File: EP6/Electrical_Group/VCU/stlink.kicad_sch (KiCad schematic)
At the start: 33 parts, among them J16 STDC14, J2 Conn_01x06, J24 USB_C_stm32, SW1 VBUS, SW2 VBUS, U1 USB3300-EZK, U14 LM66100DCK, U15 USBLC6-2SC6, Y3 X322524MSB4SI

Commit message: add silkscreen on VCU PCB
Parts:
- J16: footprint Connector_PinHeader_1.27mm:PinHeader_2x07_P1.27mm_Vertical -> nturt_kicad_lib_EP6:box_header_14P_pitch127
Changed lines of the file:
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@@
 			)
 		)
-		(property "Footprint" "Connector_PinHeader_1.27mm:PinHeader_2x07_P1.27mm_Vertical"
+		(property "Footprint" "nturt_kicad_lib_EP6:box_header_14P_pitch127"
 			(at 39.37 137.16 0)
 			(effects

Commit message: VCU snapshot
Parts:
- added R2: 100R, Resistor_SMD:R_0402_1005Metric, symbol Device:R_Small
- J2, SW2: now not fitted; now left out of the parts list
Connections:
- net 3V3_stlinkv3 is gone; now on net +3V3: J16.3 (Pin_3), SW2.1 (A)
- net GND: now also R2.1
- net at J16.11 (Pin_11): now also R2.2
- no-connect marks 13 -> 12
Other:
- note removed: "GNDDetect"
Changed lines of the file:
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@@
 	)
 	(junction
+		(at 26.67 132.08)
+		(diameter 0)
+		(color 0 0 0 0)
+	)
+	(junction
 		(at 64.77 50.8)
 		(diameter 0)
@@
 		(at 34.29 129.54)
 	)
-	(no_connect
-		(at 34.29 142.24)
-	)
 	(bus_entry
 		(at 194.31 126.746)
@@
 	(wire
 		(pts
+			(xy 21.59 142.24) (xy 34.29 142.24)
+		)
+		(stroke
+			(width 0)
+			(type default)
+		)
+	)
+	(wire
+		(pts
 			(xy 245.11 68.58) (xy 255.27 68.58)
 		)
@@
 	(wire
 		(pts
+			(xy 24.13 132.08) (xy 26.67 132.08)
+		)
+		(stroke
+			(width 0)
+			(type default)
+		)
+	)
+	(wire
+		(pts
 			(xy 242.57 27.94) (xy 255.27 27.94)
 		)
@@
 	(wire
 		(pts
+			(xy 15.24 142.24) (xy 16.51 142.24)
+		)
+		(stroke
+			(width 0)
+			(type default)
+		)
+	)
+	(wire
+		(pts
 			(xy 157.48 142.24) (xy 157.48 140.97)
 		)
@@
 		)
 	)
-	(text "GNDDetect"
-		(exclude_from_sim no)
-		(at 27.432 141.986 0)
-		(effects
-			(font
-				(size 1.27 1.27)
-			)
-		)
-	)
 	(text "NC"
 		(exclude_from_sim no)
@@
 		(at 53.34 118.11 180)
 		(unit 1)
-		(exclude_from_sim no)
-		(in_bom yes)
-		(on_board yes)
-		(dnp no)
+		(exclude_from_sim yes)
+		(in_bom no)
+		(on_board no)
+		(dnp yes)
 		(property "Reference" "SW2"
 			(at 53.34 110.49 0)
@@
 	(symbol
 		(lib_id "Device:R_Small")
+		(at 19.05 142.24 90)
+		(unit 1)
+		(exclude_from_sim no)
+		(in_bom yes)
+		(on_board yes)
+		(dnp no)
+		(fields_autoplaced yes)
+		(property "Reference" "R2"
+			(at 19.05 137.16 90)
+			(effects
+				(font
+					(size 1.27 1.27)
+				)
+			)
+		)
+		(property "Value" "100R"
+			(at 19.05 139.7 90)
+			(effects
+				(font
+					(size 1.27 1.27)
+				)
+			)
+		)
+		(property "Footprint" "Resistor_SMD:R_0402_1005Metric"
+			(at 19.05 142.24 0)
+			(effects
+				(font
+					(size 1.27 1.27)
+				)
+				(hide yes)
+			)
+		)
+		(property "Datasheet" "~"
+			(at 19.05 142.24 0)
+			(effects
+				(font
+					(size 1.27 1.27)
+				)
+				(hide yes)
+			)
+		)
+		(property "Description" "Resistor, small symbol"
+			(at 19.05 142.24 0)
+			(effects
+				(font
+					(size 1.27 1.27)
+				)
+				(hide yes)
+			)
+		)
+		(pin "2"
+		)
+		(pin "1"
+		)
+		(instances
+			(project ""
+				(path "/eb296f24-894e-4ea0-b0cd-3ba211155378/8cfc0c25-167d-4741-83fd-c9c2a0704b89"
+					(reference "R2")
+					(unit 1)
+				)
+			)
+		)
+	)
+	(symbol
+		(lib_id "Device:R_Small")
 		(at 257.81 25.4 90)
 		(unit 1)
@@
 	)
 	(symbol
+		(lib_id "power:GND")
+		(at 15.24 142.24 270)
+		(unit 1)
+		(exclude_from_sim no)
+		(in_bom yes)
+		(on_board yes)
+		(dnp no)
+		(fields_autoplaced yes)
+		(property "Reference" "#PWR042"
+			(at 8.89 142.24 0)
+			(effects
+				(font
+					(size 1.27 1.27)
+				)
+				(hide yes)
+			)
+		)
+		(property "Value" "GND"
+			(at 10.16 142.24 0)
+			(effects
+				(font
+					(size 1.27 1.27)
+				)
+				(hide yes)
+			)
+		)
+		(property "Footprint" ""
+			(at 15.24 142.24 0)
+			(effects
+				(font
+					(size 1.27 1.27)
+				)
+				(hide yes)
+			)
+		)
+		(property "Datasheet" ""
+			(at 15.24 142.24 0)
+			(effects
+				(font
+					(size 1.27 1.27)
+				)
+				(hide yes)
+			)
+		)
+		(property "Description" "Power symbol creates a global label with name \"GND\" , ground"
+			(at 15.24 142.24 0)
+			(effects
+				(font
+					(size 1.27 1.27)
+				)
+				(hide yes)
+			)
+		)
+		(pin "1"
+		)
+		(instances
+			(project "VCU"
+				(path "/eb296f24-894e-4ea0-b0cd-3ba211155378/8cfc0c25-167d-4741-83fd-c9c2a0704b89"
+					(reference "#PWR042")
+					(unit 1)
+				)
+			)
+		)
+	)
+	(symbol
 		(lib_id "Device:Crystal_GND24")
 		(at 102.87 107.95 0)
@@
 	)
 	(symbol
+		(lib_id "power:+3V3")
+		(at 24.13 132.08 90)
+		(unit 1)
+		(exclude_from_sim no)
+		(in_bom yes)
+		(on_board yes)
+		(dnp no)
+		(fields_autoplaced yes)
+		(property "Reference" "#PWR04"
+			(at 27.94 132.08 0)
+			(effects
+				(font
+					(size 1.27 1.27)
+				)
+				(hide yes)
+			)
+		)
+		(property "Value" "+3V3"
+			(at 20.32 132.0799 90)
+			(effects
+				(font
+					(size 1.27 1.27)
+				)
+				(justify left)
+			)
+		)
+		(property "Footprint" ""
+			(at 24.13 132.08 0)
+			(effects
+				(font
+					(size 1.27 1.27)
+				)
+				(hide yes)
+			)
+		)
+		(property "Datasheet" ""
+			(at 24.13 132.08 0)
+			(effects
+				(font
+					(size 1.27 1.27)
+				)
+				(hide yes)
+			)
+		)
+		(property "Description" "Power symbol creates a global label with name \"+3V3\""
+			(at 24.13 132.08 0)
+			(effects
+				(font
+					(size 1.27 1.27)
+				)
+				(hide yes)
+			)
+		)
+		(pin "1"
+		)
+		(instances
+			(project "VCU"
+				(path "/eb296f24-894e-4ea0-b0cd-3ba211155378/8cfc0c25-167d-4741-83fd-c9c2a0704b89"
+					(reference "#PWR04")
+					(unit 1)
+				)
+			)
+		)
+	)
+	(symbol
 		(lib_id "Power_Management:LM66100DCK")
 		(at 110.49 36.83 0)
@@
 		(at 38.1 102.87 180)
 		(unit 1)
-		(exclude_from_sim no)
-		(in_bom yes)
-		(on_board yes)
-		(dnp no)
+		(exclude_from_sim yes)
+		(in_bom no)
+		(on_board no)
+		(dnp yes)
 		(fields_autoplaced yes)
 		(property "Reference" "J2"

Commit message: VCU snapshot
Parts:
- R18, R52, R99: footprint Resistor_SMD:R_0603_1608Metric -> Resistor_SMD:R_0402_1005Metric
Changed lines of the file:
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@@
 			)
 		)
-		(property "Footprint" "Resistor_SMD:R_0603_1608Metric"
+		(property "Footprint" "Resistor_SMD:R_0402_1005Metric"
 			(at 259.08 111.252 90)
 			(effects
@@
 			)
 		)
-		(property "Footprint" "Resistor_SMD:R_0603_1608Metric"
+		(property "Footprint" "Resistor_SMD:R_0402_1005Metric"
 			(at 259.08 112.268 90)
 			(effects
@@
 			)
 		)
-		(property "Footprint" "Resistor_SMD:R_0603_1608Metric"
+		(property "Footprint" "Resistor_SMD:R_0402_1005Metric"
 			(at 125.222 137.16 90)
 			(effects

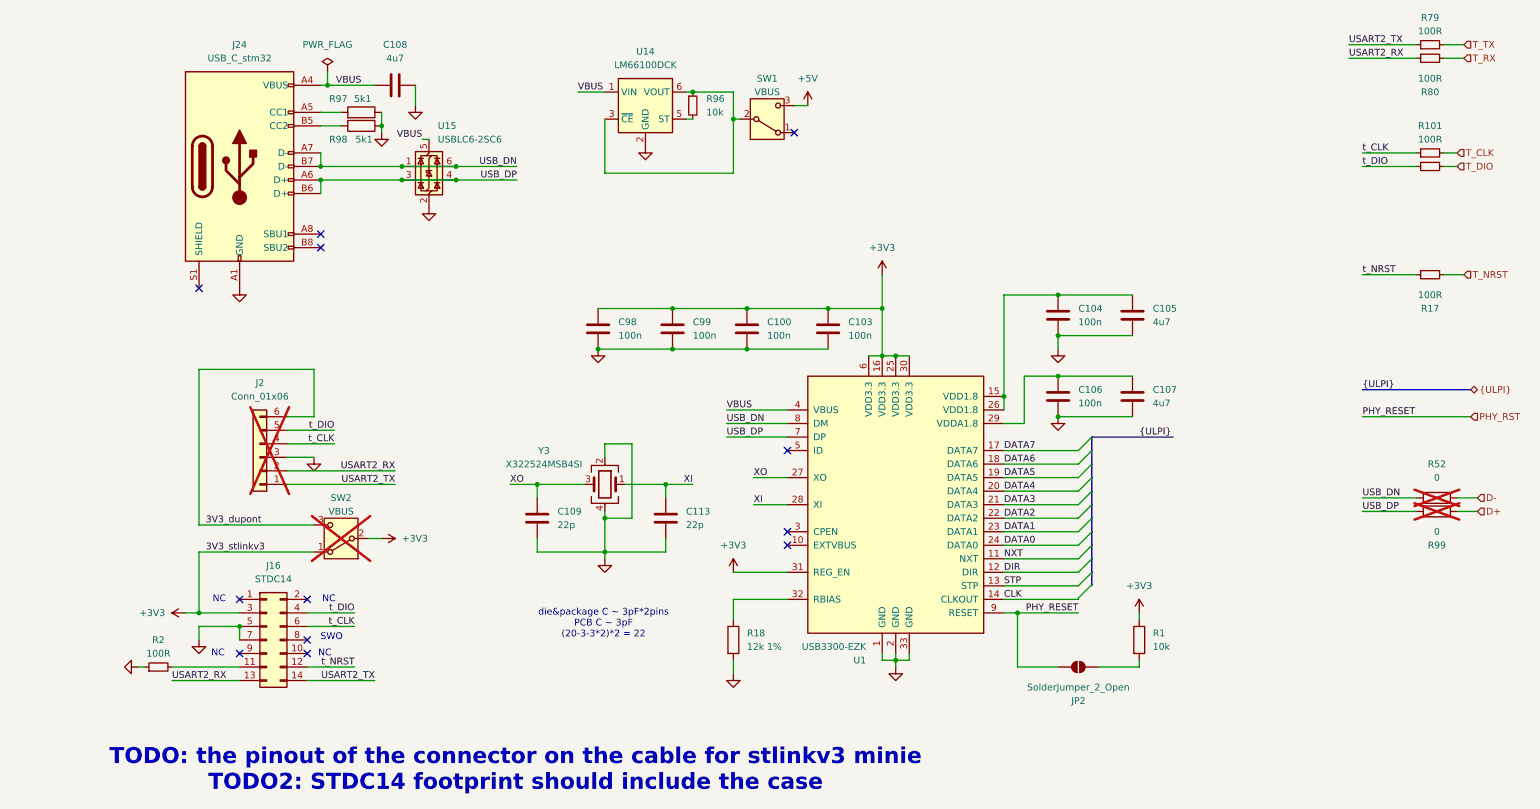
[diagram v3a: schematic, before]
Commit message: VCU initial layout
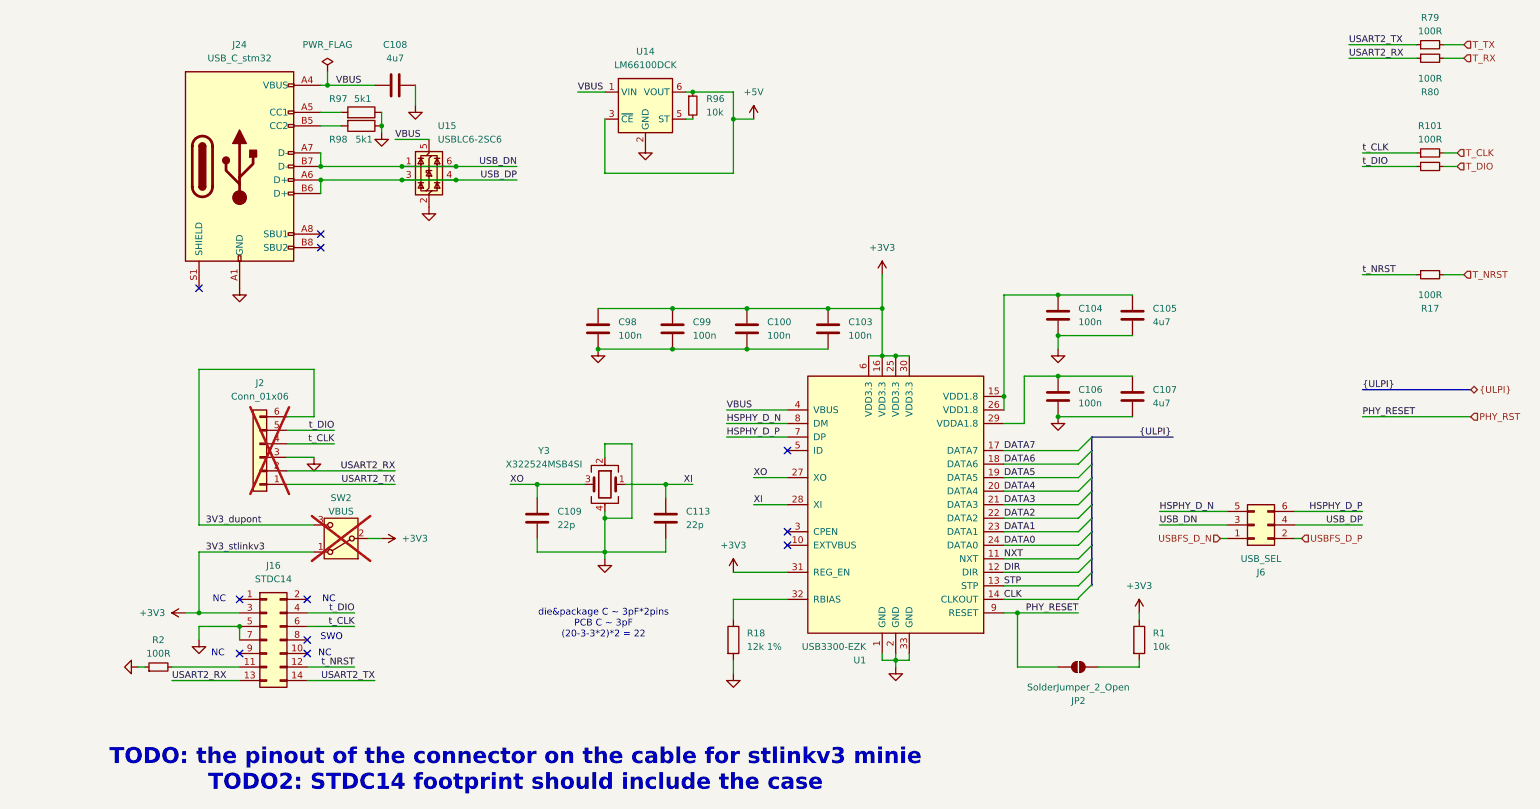
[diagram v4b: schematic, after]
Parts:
- removed R52, R99: 0, Resistor_SMD:R_0402_1005Metric, symbol Device:R
- removed SW1: VBUS, Connector_PinHeader_2.54mm:PinHeader_1x03_P2.54mm_Vertical, symbol Switch:SW_SPDT
- added J6: USB_SEL, Connector_PinHeader_2.54mm:PinHeader_2x03_P2.54mm_Vertical_SMD, symbol Connector_Generic:Conn_02x03_Odd_Even
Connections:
- net +5V: now also R96.1, U14.3 (~{CE}), U14.6 (VOUT)
- net USB_DN: now also J6.3 (Pin_3); no longer U1.8 (DM)
- net USB_DP: now also J6.4 (Pin_4); no longer U1.7 (DP)
- new net HSPHY_D_N: J6.5 (Pin_5), U1.8 (DM)
- new net HSPHY_D_P: J6.6 (Pin_6), U1.7 (DP)
- new net USBFS_D_N: J6.1 (Pin_1)
- new net USBFS_D_P: J6.2 (Pin_2)
- no-connect marks 12 -> 11

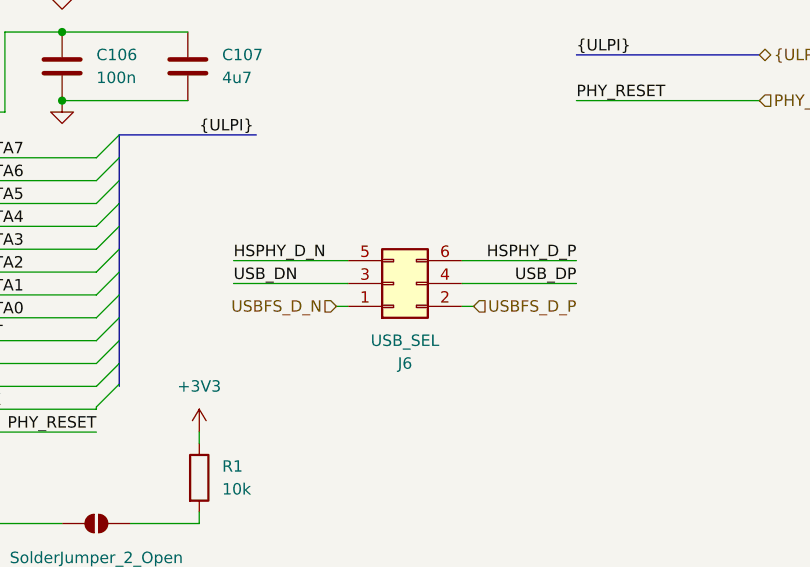
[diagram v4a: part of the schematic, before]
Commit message: VCU added silkscreen, added transfer vias, fixed ULP trace impedance
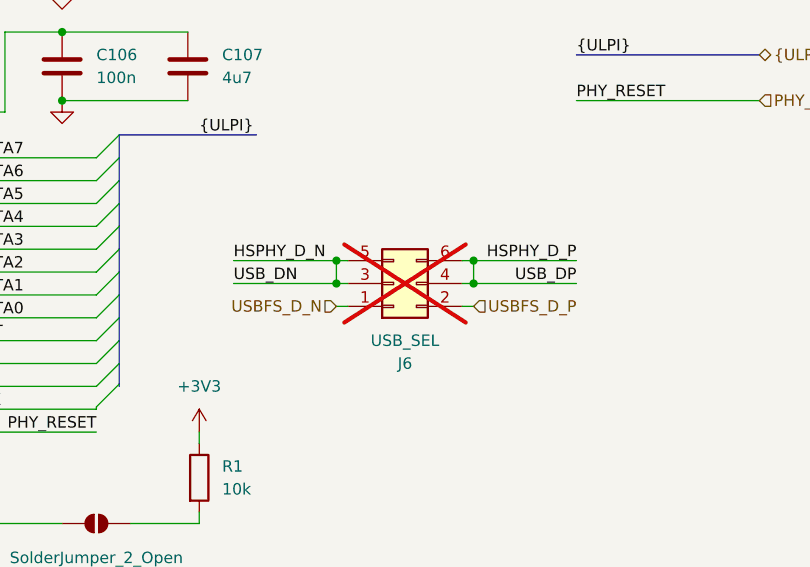
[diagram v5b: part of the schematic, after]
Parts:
- J6: now not fitted
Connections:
- net USB_DN is gone; now on net HSPHY_D_N: J24.A7 (D-), J24.B7 (D-), J6.3 (Pin_3), U15.1 (I/O1), U15.6 (I/O1)
- net USB_DP is gone; now on net HSPHY_D_P: J24.A6 (D+), J24.B6 (D+), J6.4 (Pin_4), U15.3 (I/O2), U15.4 (I/O2)
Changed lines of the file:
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@@
 	)
 	(junction
+		(at 233.68 115.57)
+		(diameter 0)
+		(color 0 0 0 0)
+	)
+	(junction
 		(at 49.53 50.8)
 		(diameter 0)
@@
 	)
 	(junction
+		(at 233.68 113.03)
+		(diameter 0)
+		(color 0 0 0 0)
+	)
+	(junction
 		(at 154.94 74.93)
 		(diameter 0)
@@
 	)
 	(junction
+		(at 218.44 113.03)
+		(diameter 0)
+		(color 0 0 0 0)
+	)
+	(junction
 		(at 115.57 82.55)
 		(diameter 0)
@@
 	)
 	(junction
+		(at 218.44 115.57)
+		(diameter 0)
+		(color 0 0 0 0)
+	)
+	(junction
 		(at 119.38 34.29)
 		(diameter 0)
@@
 	(wire
 		(pts
-			(xy 232.41 115.57) (xy 245.11 115.57)
+			(xy 232.41 115.57) (xy 233.68 115.57)
 		)
 		(stroke
@@
 	(wire
 		(pts
+			(xy 218.44 115.57) (xy 219.71 115.57)
+		)
+		(stroke
+			(width 0)
+			(type default)
+		)
+	)
+	(wire
+		(pts
 			(xy 64.77 50.8) (xy 74.93 50.8)
 		)
@@
 	(wire
 		(pts
+			(xy 218.44 113.03) (xy 219.71 113.03)
+		)
+		(stroke
+			(width 0)
+			(type default)
+		)
+	)
+	(wire
+		(pts
 			(xy 137.16 129.54) (xy 127 129.54)
 		)
@@
 	(wire
 		(pts
+			(xy 218.44 113.03) (xy 218.44 115.57)
+		)
+		(stroke
+			(width 0)
+			(type default)
+		)
+	)
+	(wire
+		(pts
 			(xy 130.81 111.76) (xy 137.16 111.76)
 		)
@@
 	(wire
 		(pts
+			(xy 233.68 115.57) (xy 245.11 115.57)
+		)
+		(stroke
+			(width 0)
+			(type default)
+		)
+	)
+	(wire
+		(pts
 			(xy 177.8 132.08) (xy 180.34 132.08)
 		)
@@
 	(wire
 		(pts
+			(xy 233.68 113.03) (xy 233.68 115.57)
+		)
+		(stroke
+			(width 0)
+			(type default)
+		)
+	)
+	(wire
+		(pts
 			(xy 260.35 45.72) (xy 262.89 45.72)
 		)
@@
 	(wire
 		(pts
-			(xy 207.01 113.03) (xy 219.71 113.03)
+			(xy 207.01 113.03) (xy 218.44 113.03)
 		)
 		(stroke
@@
 	(wire
 		(pts
+			(xy 233.68 113.03) (xy 245.11 113.03)
+		)
+		(stroke
+			(width 0)
+			(type default)
+		)
+	)
+	(wire
+		(pts
 			(xy 157.48 142.24) (xy 157.48 140.97)
 		)
@@
 	(wire
 		(pts
-			(xy 207.01 115.57) (xy 219.71 115.57)
+			(xy 207.01 115.57) (xy 218.44 115.57)
 		)
 		(stroke
@@
 	(wire
 		(pts
-			(xy 232.41 113.03) (xy 245.11 113.03)
+			(xy 232.41 113.03) (xy 233.68 113.03)
 		)
 		(stroke
@@
 		(in_bom yes)
 		(on_board yes)
-		(dnp no)
+		(dnp yes)
 		(property "Reference" "J6"
 			(at 226.06 124.46 0)
